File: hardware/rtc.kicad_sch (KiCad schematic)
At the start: 4 parts, among them IC1 DS3234S#

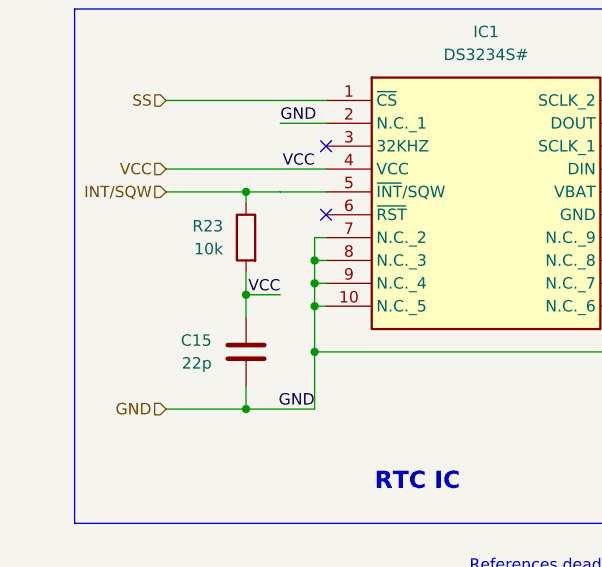
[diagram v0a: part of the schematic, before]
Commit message: organized schem and updated readme
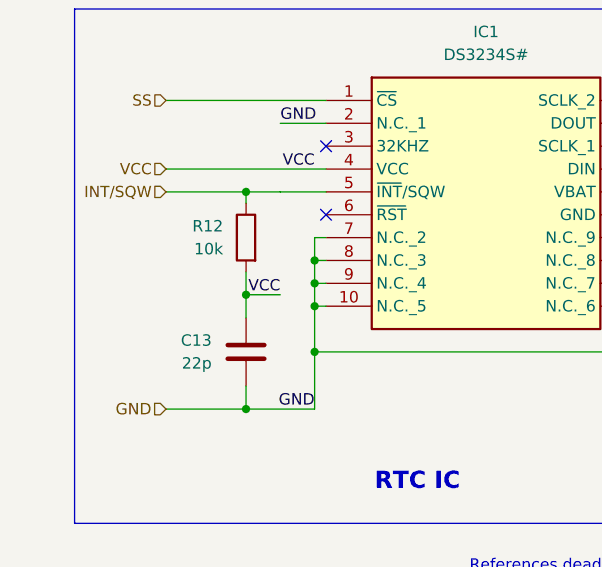
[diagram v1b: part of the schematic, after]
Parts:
- renumbered C15 to C13, R23 to R12
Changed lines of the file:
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@@
 		(on_board yes)
 		(dnp no)
-		(property "Reference" "C15"
+		(property "Reference" "C13"
 			(at 96.52 104.1399 0)
 			(effects
@@
 			(project "BREAD_Slice"
 				(path "/66043bca-a260-4915-9fce-8a51d324c687/e694580f-4afe-4f66-ab5c-4cae81fec964"
-					(reference "C15")
+					(reference "C13")
 					(unit 1)
 				)
@@
 		(on_board yes)
 		(dnp no)
-		(property "Reference" "R23"
+		(property "Reference" "R12"
 			(at 97.79 91.4399 0)
 			(effects
@@
 			(project "BREAD_Slice"
 				(path "/66043bca-a260-4915-9fce-8a51d324c687/e694580f-4afe-4f66-ab5c-4cae81fec964"
-					(reference "R23")
+					(reference "R12")
 					(unit 1)
 				)

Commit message: completed board
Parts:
- removed BAT1: 3V, DeadOn RTC - DS3234 Breakout-v11:BATTCON_12MM_CURVED, symbol DeadOn RTC - DS3234 Breakout-v11-eagle-import:BATTERY
- added BT1: Battery_Cell, Battery:BatteryHolder_Keystone_3000_1x12mm, symbol Device:Battery_Cell
- C13: footprint (none) -> Capacitor_SMD:C_1206_3216Metric_Pad1.33x1.80mm_HandSolder
- IC1: footprint SOIC127P1032X265-20N -> KML-Custom:SOIC127P1032X265-20N
- R15: renamed from R12; footprint (none) -> Resistor_SMD:R_1206_3216Metric_Pad1.30x1.75mm_HandSolder
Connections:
- net GND: now also BT1.2 (-)
- net VBATT: now also BT1.1 (+)
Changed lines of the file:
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@@
 	(wire
 		(pts
-			(xy 193.04 83.82) (xy 193.04 86.36)
+			(xy 193.04 83.82) (xy 193.04 87.63)
 		)
 		(stroke
@@
 	(wire
 		(pts
-			(xy 193.04 96.52) (xy 193.04 99.06)
+			(xy 151.13 87.63) (xy 144.78 87.63)
+		)
+		(stroke
+			(width 0)
+			(type default)
+		)
+	)
+	(wire
+		(pts
+			(xy 146.05 92.71) (xy 146.05 95.25)
+		)
+		(stroke
+			(width 0)
+			(type default)
+		)
+	)
+	(wire
+		(pts
+			(xy 100.33 111.76) (xy 100.33 109.22)
+		)
+		(stroke
+			(width 0)
+			(type default)
+		)
+	)
+	(wire
+		(pts
+			(xy 146.05 95.25) (xy 146.05 97.79)
+		)
+		(stroke
+			(width 0)
+			(type default)
+		)
+	)
+	(wire
+		(pts
+			(xy 146.05 100.33) (xy 144.78 100.33)
+		)
+		(stroke
+			(width 0)
+			(type default)
+		)
+	)
+	(wire
+		(pts
+			(xy 100.33 99.06) (xy 100.33 101.6)
 		)
 		(stroke
@@
 	(wire
 		(pts
-			(xy 151.13 87.63) (xy 144.78 87.63)
-		)
-		(stroke
-			(width 0)
-			(type default)
-		)
-	)
-	(wire
-		(pts
-			(xy 146.05 92.71) (xy 146.05 95.25)
-		)
-		(stroke
-			(width 0)
-			(type default)
-		)
-	)
-	(wire
-		(pts
-			(xy 100.33 111.76) (xy 100.33 109.22)
-		)
-		(stroke
-			(width 0)
-			(type default)
-		)
-	)
-	(wire
-		(pts
-			(xy 146.05 95.25) (xy 146.05 97.79)
-		)
-		(stroke
-			(width 0)
-			(type default)
-		)
-	)
-	(wire
-		(pts
-			(xy 146.05 100.33) (xy 144.78 100.33)
-		)
-		(stroke
-			(width 0)
-			(type default)
-		)
-	)
-	(wire
-		(pts
-			(xy 100.33 99.06) (xy 100.33 101.6)
+			(xy 107.95 97.79) (xy 107.95 100.33)
+		)
+		(stroke
+			(width 0)
+			(type default)
+		)
+	)
+	(wire
+		(pts
+			(xy 177.8 83.82) (xy 193.04 83.82)
 		)
 		(stroke
@@
 	(wire
 		(pts
-			(xy 107.95 97.79) (xy 107.95 100.33)
-		)
-		(stroke
-			(width 0)
-			(type default)
-		)
-	)
-	(wire
-		(pts
-			(xy 177.8 83.82) (xy 193.04 83.82)
+			(xy 146.05 92.71) (xy 144.78 92.71)
+		)
+		(stroke
+			(width 0)
+			(type default)
+		)
+	)
+	(wire
+		(pts
+			(xy 156.21 85.09) (xy 144.78 85.09)
+		)
+		(stroke
+			(width 0)
+			(type default)
+		)
+	)
+	(wire
+		(pts
+			(xy 146.05 100.33) (xy 146.05 105.41)
+		)
+		(stroke
+			(width 0)
+			(type default)
+		)
+	)
+	(wire
+		(pts
+			(xy 104.14 87.63) (xy 100.33 87.63)
 		)
 		(stroke
@@
 	(wire
 		(pts
-			(xy 146.05 92.71) (xy 144.78 92.71)
-		)
-		(stroke
-			(width 0)
-			(type default)
-		)
-	)
-	(wire
-		(pts
-			(xy 156.21 85.09) (xy 144.78 85.09)
-		)
-		(stroke
-			(width 0)
-			(type default)
-		)
-	)
-	(wire
-		(pts
-			(xy 146.05 100.33) (xy 146.05 105.41)
-		)
-		(stroke
-			(width 0)
-			(type default)
-		)
-	)
-	(wire
-		(pts
-			(xy 104.14 87.63) (xy 100.33 87.63)
+			(xy 146.05 90.17) (xy 146.05 92.71)
+		)
+		(stroke
+			(width 0)
+			(type default)
+		)
+	)
+	(wire
+		(pts
+			(xy 107.95 105.41) (xy 107.95 111.76)
+		)
+		(stroke
+			(width 0)
+			(type default)
+		)
+	)
+	(wire
+		(pts
+			(xy 193.04 95.25) (xy 193.04 99.06)
 		)
 		(stroke
 			(width 0.1524)
 			(type solid)
-		)
-	)
-	(wire
-		(pts
-			(xy 146.05 90.17) (xy 146.05 92.71)
-		)
-		(stroke
-			(width 0)
-			(type default)
-		)
-	)
-	(wire
-		(pts
-			(xy 107.95 105.41) (xy 107.95 111.76)
-		)
-		(stroke
-			(width 0)
-			(type default)
 		)
 	)
@@
 			)
 		)
-		(property "Footprint" "SOIC127P1032X265-20N"
+		(property "Footprint" "KML-Custom:SOIC127P1032X265-20N"
 			(at 140.97 172.39 0)
 			(effects
@@
 			)
 		)
-		(property "Footprint" ""
+		(property "Footprint" "Capacitor_SMD:C_1206_3216Metric_Pad1.33x1.80mm_HandSolder"
 			(at 99.3648 109.22 0)
 			(effects
@@
 				(path "/66043bca-a260-4915-9fce-8a51d324c687/e694580f-4afe-4f66-ab5c-4cae81fec964"
 					(reference "C13")
+					(unit 1)
+				)
+			)
+		)
+	)
+	(symbol
+		(lib_id "Device:Battery_Cell")
+		(at 193.04 92.71 0)
+		(unit 1)
+		(exclude_from_sim no)
+		(in_bom yes)
+		(on_board yes)
+		(dnp no)
+		(fields_autoplaced yes)
+		(property "Reference" "BT1"
+			(at 196.85 89.5984 0)
+			(effects
+				(font
+					(size 1.27 1.27)
+				)
+				(justify left)
+			)
+		)
+		(property "Value" "Battery_Cell"
+			(at 196.85 92.1384 0)
+			(effects
+				(font
+					(size 1.27 1.27)
+				)
+				(justify left)
+			)
+		)
+		(property "Footprint" "Battery:BatteryHolder_Keystone_3000_1x12mm"
+			(at 193.04 91.186 90)
+			(effects
+				(font
+					(size 1.27 1.27)
+				)
+				(hide yes)
+			)
+		)
+		(property "Datasheet" "~"
+			(at 193.04 91.186 90)
+			(effects
+				(font
+					(size 1.27 1.27)
+				)
+				(hide yes)
+			)
+		)
+		(property "Description" "Single-cell battery"
+			(at 193.04 92.71 0)
+			(effects
+				(font
+					(size 1.27 1.27)
+				)
+				(hide yes)
+			)
+		)
+		(pin "2"
+		)
+		(pin "1"
+		)
+		(instances
+			(project "BREAD_Slice"
+				(path "/66043bca-a260-4915-9fce-8a51d324c687/e694580f-4afe-4f66-ab5c-4cae81fec964"
+					(reference "BT1")
 					(unit 1)
 				)
@@
 		(on_board yes)
 		(dnp no)
-		(property "Reference" "R12"
+		(property "Reference" "R15"
 			(at 97.79 91.4399 0)
 			(effects
@@
 			)
 		)
-		(property "Footprint" ""
+		(property "Footprint" "Resistor_SMD:R_1206_3216Metric_Pad1.30x1.75mm_HandSolder"
 			(at 102.108 92.71 90)
 			(effects
@@
 			(project "BREAD_Slice"
 				(path "/66043bca-a260-4915-9fce-8a51d324c687/e694580f-4afe-4f66-ab5c-4cae81fec964"
-					(reference "R12")
+					(reference "R15")
 					(unit 1)
 				)
-			)
-		)
-	)
-	(symbol
-		(lib_id "DeadOn RTC - DS3234 Breakout-v11-eagle-import:BATTERY")
-		(at 193.04 91.44 270)
-		(unit 1)
-		(exclude_from_sim no)
-		(in_bom yes)
-		(on_board yes)
-		(dnp no)
-		(property "Reference" "BAT1"
-			(at 198.12 87.63 0)
-			(effects
-				(font
-					(size 1.778 1.5113)
-				)
-				(justify left bottom)
-			)
-		)
-		(property "Value" "3V"
-			(at 186.69 87.63 0)
-			(effects
-				(font
-					(size 1.778 1.5113)
-				)
-				(justify left bottom)
-			)
-		)
-		(property "Footprint" "DeadOn RTC - DS3234 Breakout-v11:BATTCON_12MM_CURVED"
-			(at 193.04 91.44 0)
-			(effects
-				(font
-					(size 1.27 1.27)
-				)
-				(hide yes)
-			)
-		)
-		(property "Datasheet" ""
-			(at 193.04 91.44 0)
-			(effects
-				(font
-					(size 1.27 1.27)
-				)
-				(hide yes)
-			)
-		)
-		(property "Description" ""
-			(at 193.04 91.44 0)
-			(effects
-				(font
-					(size 1.27 1.27)
-				)
-				(hide yes)
-			)
-		)
-		(pin "GND"
-		)
-		(pin "PWR@1"
-		)
-		(instances
-			(project "BREAD_Slice"
-				(path "/66043bca-a260-4915-9fce-8a51d324c687/e694580f-4afe-4f66-ab5c-4cae81fec964"
-					(reference "BAT1")
-					(unit 1)
-				)
